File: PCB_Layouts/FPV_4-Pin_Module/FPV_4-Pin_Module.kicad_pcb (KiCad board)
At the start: 2 copper layers, 33.5 x 25.2 mm, 4 parts, among them J1 Conn_01x04_Socket, J2 Conn_01x10_Socket, J3 Conn_01x10_Socket

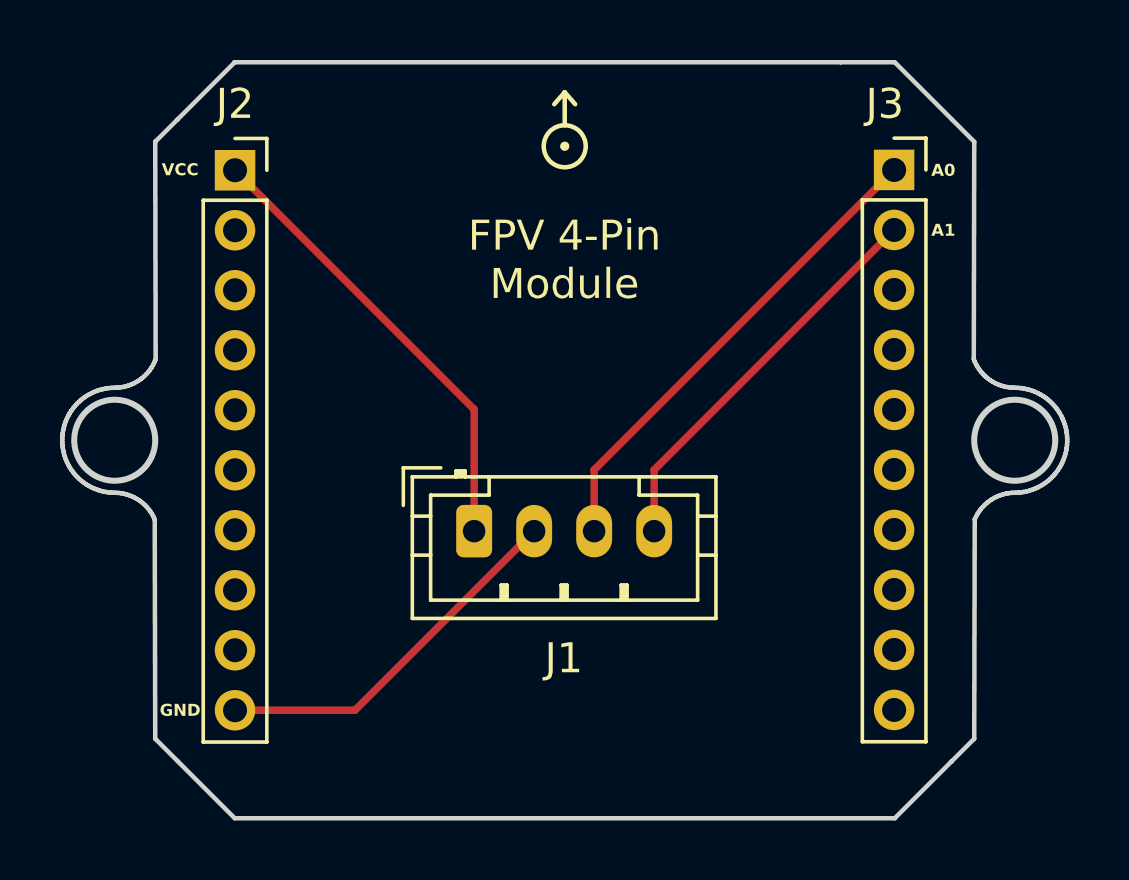
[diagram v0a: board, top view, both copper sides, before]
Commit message: Adding FPV 4 Pin quote
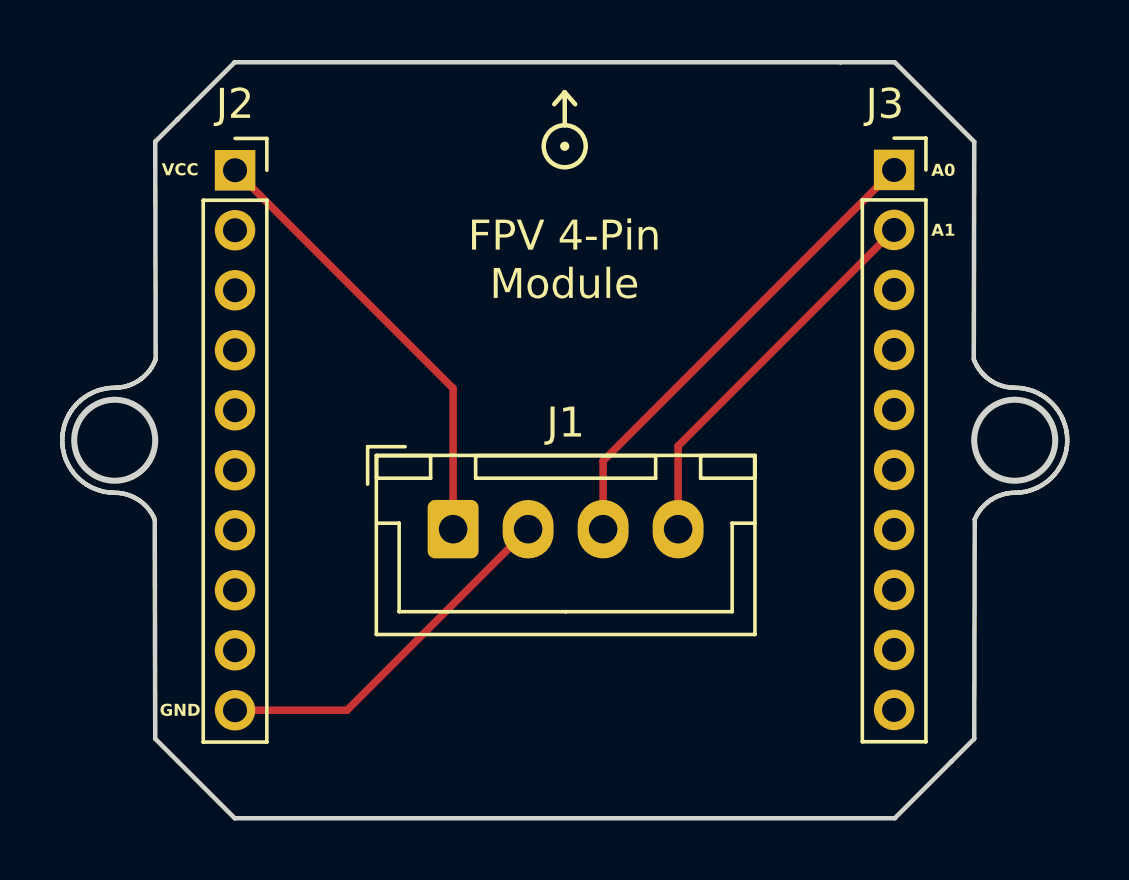
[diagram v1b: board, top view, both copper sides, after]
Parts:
- J1: footprint Connector_JST:JST_PH_B4B-PH-K_1x04_P2.00mm_Vertical -> Connector_JST:JST_XH_B4B-XH-A_1x04_P2.50mm_Vertical
- moved J1 0.70 mm to (145.6, 83.2)
